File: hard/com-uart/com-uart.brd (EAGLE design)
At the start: 76 x 22 mm, 10 parts, among them J1 J0006D21

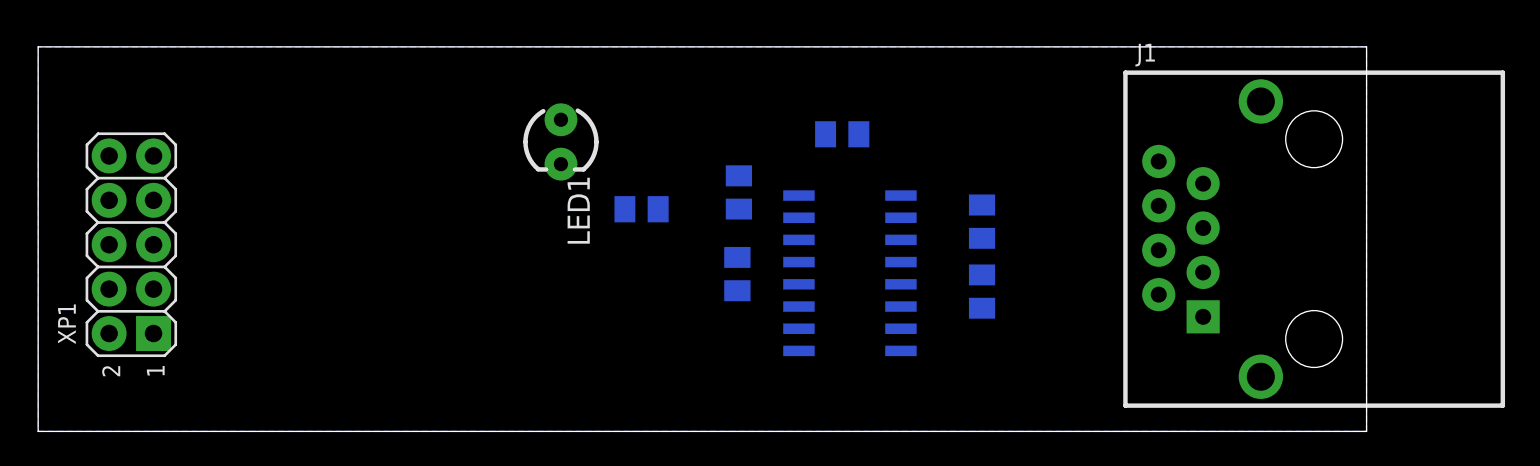
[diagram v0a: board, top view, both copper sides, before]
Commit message: almost finished pcb for com-uart
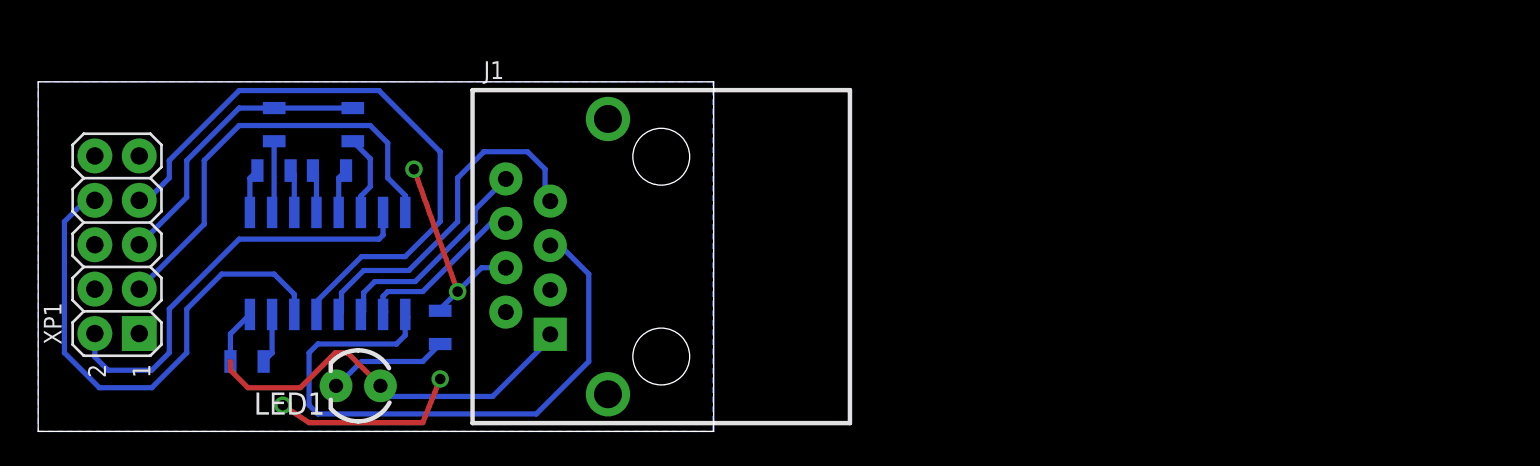
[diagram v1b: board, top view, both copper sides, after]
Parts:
- C1, C2, C3, C4, C5: device rcl:C0805 -> barthess:0805
- R1: device rcl:R0805 -> barthess:0805
- moved C1 40.6 mm to (13.5, 14.9), turned to 180 degrees
- moved C2 37.9 mm to (16.7, 14.9), turned to 180 degrees
- moved J1 37.4 mm to (35.6, 10.0)
- moved C4 32.5 mm to (13.5, 17.5), turned to 270 degrees
- moved DA7 29.9 mm to (16.6, 9.61), turned to 180 degrees
- moved C5 29.7 mm to (12.0, 4.00), turned to 180 degrees
- moved C3 23.6 mm to (18.0, 17.5)
- moved LED1 18.1 mm to (18.3, 2.61), turned to 180 degrees
- moved R1 13.3 mm to (23.0, 6.00), turned to 90 degrees
- moved XP1 0.82 mm to (5.78, 5.60)
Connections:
- removed net USART_FROM_MCU: DA7.10
- removed net USART_TO_MCU: DA7.9
- new net CMOS_CTS: DA7.12, J1.7
- new net CMOS_FROM_MCU: DA7.10, J1.6
- new net CMOS_RTS: DA7.11, J1.8
- new net CMOS_TO_MCU: DA7.9, J1.5
- new net CTS_RS232: DA7.14, XP1.8
- new net RTS_RS232: DA7.13, XP1.7
- net +3V3: now also J1.1
- net FROM_RS232: now also XP1.3
- net GND: now also J1.4, XP1.5
- net TO_RS232: now also XP1.2
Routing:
- net GND: track 0.00 -> 42.7 mm, vias 0 -> 4
- net RTS_RS232: track 0.00 -> 35.6 mm
- net CMOS_TO_MCU: track 0.00 -> 35.5 mm
- net CTS_RS232: track 0.00 -> 29.8 mm
- net +3V3: track 0.00 -> 26.0 mm
- net FROM_RS232: track 0.00 -> 25.0 mm
- net TO_RS232: track 0.00 -> 24.1 mm
- net CMOS_CTS: track 0.00 -> 20.1 mm
- net CMOS_RTS: track 0.00 -> 12.5 mm
- net CMOS_FROM_MCU: track 0.00 -> 10.0 mm
- net N$1: track 0.00 -> 6.95 mm
- net N$235: track 0.00 -> 4.71 mm
- net N$233: track 0.00 -> 4.12 mm
- net N$239: track 0.00 -> 2.57 mm
- net N$241: track 0.00 -> 2.57 mm
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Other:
- board size 76 x 22 mm -> 38.6 x 20 mm

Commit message: nop
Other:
- board size 38.6 x 20 mm -> 41.6 x 20 mm
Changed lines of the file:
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@@
 <board>
 <plain>
-<wire x1="0" y1="0" x2="38.6475" y2="0" width="0" layer="20"/>
-<wire x1="38.6475" y1="0" x2="38.6475" y2="20" width="0" layer="20"/>
-<wire x1="38.6475" y1="20" x2="0" y2="20" width="0" layer="20"/>
+<wire x1="0" y1="0" x2="41.6475" y2="0" width="0" layer="20"/>
+<wire x1="41.6475" y1="0" x2="41.6475" y2="20" width="0" layer="20"/>
+<wire x1="41.6475" y1="20" x2="0" y2="20" width="0" layer="20"/>
 <wire x1="0" y1="20" x2="0" y2="0" width="0" layer="20"/>
 </plain>
@@
 <polygon width="0.3" layer="16" isolate="0.4" orphans="yes">
 <vertex x="0" y="0"/>
-<vertex x="38.585" y="0"/>
-<vertex x="38.585" y="20"/>
+<vertex x="41.585" y="0"/>
+<vertex x="41.585" y="20"/>
 <vertex x="0" y="20"/>
 </polygon>
@@
 <wire x1="22" y1="0.5" x2="15.5" y2="0.5" width="0.3" layer="1"/>
 <wire x1="15.5" y1="0.5" x2="14" y2="1.5" width="0.3" layer="1"/>
-<wire x1="26.7575" y1="9.365" x2="32.5995" y2="2.126" width="0" layer="19" extent="1-1"/>
+<wire x1="26.7575" y1="9.365" x2="38.9495" y2="2.126" width="0" layer="19" extent="1-1"/>
 </signal>
 <signal name="N$233">
